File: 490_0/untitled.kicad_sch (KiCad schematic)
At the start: 31 parts, among them J2 PAD, J3 PAD, U16 SP3003-02XTG, U17 SP3003-02XTG, U4 USB2512B-I/M2, Y1 24M20P2/XT324-10/10

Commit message: Changed all the resistors to 0805 size
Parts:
- R11: footprint Resistor_THT:R_Axial_DIN0207_L6.3mm_D2.5mm_P10.16mm_Horizontal -> Resistor_SMD:R_0805_2012Metric; Digikey Link https://www.digikey.ca/en/products/detail/yageo/RC1206FR-07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 -> https://www.digikey.ca/en/products/detail/yageo/RC0805FR-13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; Manufacturer Part RC1206FR-0710KL -> RC0805FR-13330RL; Package 1206 -> 0805; Supplier P/N 311-10.0KFRCT-ND -> 13-RC0805FR-13330RLCT-ND; Unit (none) -> pcs
- R41: footprint Resistor_SMD:R_0603_1608Metric -> Resistor_SMD:R_0805_2012Metric; Digikey Link https://www.digikey.ca/en/products/detail/yageo/RC1206FR-07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 -> https://www.digikey.ca/en/products/detail/yageo/RC0805FR-07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; Manufacturer Part RC1206FR-071K5L -> RC0805FR-071K5L; Package 1206 -> 0805; Supplier P/N 311-1.50KFRCT-ND -> 311-1.50KCRCT-ND
- R42, R43, R46: footprint Resistor_THT:R_Axial_DIN0207_L6.3mm_D2.5mm_P10.16mm_Horizontal -> Resistor_SMD:R_0805_2012Metric; Digikey Link https://www.digikey.ca/en/products/detail/yageo/RC1206FR-07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 -> https://www.digikey.ca/en/products/detail/yageo/RC0805FR-07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; Manufacturer Part RC1206FR-0710KL -> RC0805FR-0710KL; Package 1206 -> 0805; Price 0.1 -> 0.14; Supplier P/N 311-10.0KFRCT-ND -> 311-10.0KCRCT-ND
- R45: footprint Resistor_SMD:R_0603_1608Metric -> Resistor_SMD:R_0805_2012Metric; Digikey Link https://www.digikey.ca/en/products/detail/yageo/RC1206FR-07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 -> https://www.digikey.ca/en/products/detail/yageo/RC0805FR-07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; Manufacturer Part RC1206FR-0710KL -> RC0805FR-0710KL; Package 1206 -> 0805; Price 0.1 -> 0.14; Supplier P/N 311-10.0KFRCT-ND -> 311-10.0KCRCT-ND
- R7: footprint Resistor_SMD:R_0603_1608Metric -> Resistor_SMD:R_0805_2012Metric; Digikey Link https://www.digikey.ca/en/products/detail/yageo/RC1206FR-07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 -> https://www.digikey.ca/en/products/detail/yageo/RC0805FR-07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; Manufacturer Part RC1206FR-0712KL -> RC0805FR-0712KL; Package 1206 -> 0805; Supplier P/N 311-12.0KFRCT-ND -> 311-12.0KCRCT-ND
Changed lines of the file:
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@@
 			)
 		)
-		(property "Footprint" "Resistor_SMD:R_0603_1608Metric"
+		(property "Footprint" "Resistor_SMD:R_0805_2012Metric"
 			(at 72.898 161.29 90)
 			(effects
@@
 			)
 		)
-		(property "Description" "RES 1.5K OHM 1% 1/4W 1206"
+		(property "Description" "RES 1.5K OHM 1% 1/8W 0805"
 			(at 71.12 161.29 0)
 			(effects
@@
 			)
 		)
-		(property "Digikey Link" "https://www.digikey.ca/en/products/detail/yageo/RC1206FR-071K5L/728441"
+		(property "Digikey Link" "https://www.digikey.ca/en/products/detail/yageo/RC0805FR-071K5L/727496"
 			(at 71.12 161.29 90)
 			(effects
@@
 			)
 		)
-		(property "Manufacturer Part" "RC1206FR-071K5L"
+		(property "Manufacturer Part" "RC0805FR-071K5L"
 			(at 71.12 161.29 90)
 			(effects
@@
 			)
 		)
-		(property "Supplier P/N" "311-1.50KFRCT-ND"
+		(property "Supplier P/N" "311-1.50KCRCT-ND"
 			(at 71.12 161.29 90)
 			(effects
@@
 			)
 		)
-		(property "Package" "1206"
+		(property "Package" "0805"
 			(at 71.12 161.29 90)
 			(effects
@@
 			)
 		)
-		(property "Footprint" "Resistor_THT:R_Axial_DIN0207_L6.3mm_D2.5mm_P10.16mm_Horizontal"
+		(property "Footprint" "Resistor_SMD:R_0805_2012Metric"
 			(at 88.138 173.101 0)
 			(effects
@@
 			)
 		)
-		(property "Description" "RES 10K OHM 1% 1/4W 1206"
+		(property "Description" "RES 10K OHM 1% 1/8W 0805"
 			(at 83.82 173.99 0)
 			(effects
@@
 			)
 		)
-		(property "Digikey Link" "https://www.digikey.ca/en/products/detail/yageo/RC1206FR-0710KL/728483"
+		(property "Digikey Link" "https://www.digikey.ca/en/products/detail/yageo/RC0805FR-0710KL/727535"
 			(at 83.82 173.99 0)
 			(effects
@@
 			)
 		)
-		(property "Manufacturer Part" "RC1206FR-0710KL"
+		(property "Manufacturer Part" "RC0805FR-0710KL"
 			(at 83.82 173.99 0)
 			(effects
@@
 			)
 		)
-		(property "Package" "1206"
+		(property "Package" "0805"
 			(at 83.82 173.99 0)
 			(effects
@@
 			)
 		)
-		(property "Price" "0.1"
+		(property "Price" "0.14"
 			(at 83.82 173.99 0)
 			(effects
@@
 			)
 		)
-		(property "Supplier P/N" "311-10.0KFRCT-ND"
+		(property "Supplier P/N" "311-10.0KCRCT-ND"
 			(at 83.82 173.99 0)
 			(effects
@@
 			)
 		)
-		(property "Footprint" "Resistor_THT:R_Axial_DIN0207_L6.3mm_D2.5mm_P10.16mm_Horizontal"
+		(property "Footprint" "Resistor_SMD:R_0805_2012Metric"
 			(at 44.958 160.401 0)
 			(effects
@@
 			)
 		)
-		(property "Description" "RES 10K OHM 1% 1/4W 1206"
+		(property "Description" "RES 10K OHM 1% 1/8W 0805"
 			(at 40.64 161.29 0)
 			(effects
@@
 			)
 		)
-		(property "Digikey Link" "https://www.digikey.ca/en/products/detail/yageo/RC1206FR-0710KL/728483"
+		(property "Digikey Link" "https://www.digikey.ca/en/products/detail/yageo/RC0805FR-0710KL/727535"
 			(at 40.64 161.29 0)
 			(effects
@@
 			)
 		)
-		(property "Manufacturer Part" "RC1206FR-0710KL"
+		(property "Manufacturer Part" "RC0805FR-0710KL"
 			(at 40.64 161.29 0)
 			(effects
@@
 			)
 		)
-		(property "Package" "1206"
+		(property "Package" "0805"
 			(at 40.64 161.29 0)
 			(effects
@@
 			)
 		)
-		(property "Price" "0.1"
+		(property "Price" "0.14"
 			(at 40.64 161.29 0)
 			(effects
@@
 			)
 		)
-		(property "Supplier P/N" "311-10.0KFRCT-ND"
+		(property "Supplier P/N" "311-10.0KCRCT-ND"
 			(at 40.64 161.29 0)
 			(effects
@@
 			)
 		)
-		(property "Footprint" "Resistor_SMD:R_0603_1608Metric"
+		(property "Footprint" "Resistor_SMD:R_0805_2012Metric"
 			(at 39.878 105.41 90)
 			(effects
@@
 			)
 		)
-		(property "Description" "RES 10K OHM 1% 1/4W 1206"
+		(property "Description" "RES 10K OHM 1% 1/8W 0805"
 			(at 38.1 105.41 0)
 			(effects
@@
 			)
 		)
-		(property "Digikey Link" "https://www.digikey.ca/en/products/detail/yageo/RC1206FR-0710KL/728483"
+		(property "Digikey Link" "https://www.digikey.ca/en/products/detail/yageo/RC0805FR-0710KL/727535"
 			(at 38.1 105.41 90)
 			(effects
@@
 			)
 		)
-		(property "Manufacturer Part" "RC1206FR-0710KL"
+		(property "Manufacturer Part" "RC0805FR-0710KL"
 			(at 38.1 105.41 90)
 			(effects
@@
 			)
 		)
-		(property "Supplier P/N" "311-10.0KFRCT-ND"
+		(property "Supplier P/N" "311-10.0KCRCT-ND"
 			(at 38.1 105.41 90)
 			(effects
@@
 			)
 		)
-		(property "Package" "1206"
+		(property "Package" "0805"
 			(at 38.1 105.41 90)
 			(effects
@@
 			)
 		)
-		(property "Price" "0.1"
+		(property "Price" "0.14"
 			(at 38.1 105.41 90)
 			(effects
@@
 			)
 		)
-		(property "Footprint" "Resistor_THT:R_Axial_DIN0207_L6.3mm_D2.5mm_P10.16mm_Horizontal"
+		(property "Footprint" "Resistor_SMD:R_0805_2012Metric"
 			(at 80.518 185.801 0)
 			(effects
@@
 			)
 		)
-		(property "Description" "RES 10K OHM 1% 1/4W 1206"
+		(property "Description" "RES 330 OHM 1% 1/8W 0805"
 			(at 76.2 186.69 0)
 			(effects
@@
 			)
 		)
-		(property "Digikey Link" "https://www.digikey.ca/en/products/detail/yageo/RC1206FR-0710KL/728483"
+		(property "Digikey Link" "https://www.digikey.ca/en/products/detail/yageo/RC0805FR-13330RL/14286486"
 			(at 76.2 186.69 0)
 			(effects
@@
 			)
 		)
-		(property "Manufacturer Part" "RC1206FR-0710KL"
+		(property "Manufacturer Part" "RC0805FR-13330RL"
 			(at 76.2 186.69 0)
 			(effects
@@
 			)
 		)
-		(property "Package" "1206"
+		(property "Package" "0805"
 			(at 76.2 186.69 0)
 			(effects
@@
 			)
 		)
-		(property "Supplier P/N" "311-10.0KFRCT-ND"
+		(property "Supplier P/N" "13-RC0805FR-13330RLCT-ND"
 			(at 76.2 186.69 0)
 			(effects
@@
 			)
 		)
-		(property "Unit" ""
+		(property "Unit" "pcs"
 			(at 76.2 186.69 0)
 			(effects
@@
 			)
 		)
-		(property "Footprint" "Resistor_THT:R_Axial_DIN0207_L6.3mm_D2.5mm_P10.16mm_Horizontal"
+		(property "Footprint" "Resistor_SMD:R_0805_2012Metric"
 			(at 60.198 160.401 0)
 			(effects
@@
 			)
 		)
-		(property "Description" "RES 10K OHM 1% 1/4W 1206"
+		(property "Description" "RES 10K OHM 1% 1/8W 0805"
 			(at 55.88 161.29 0)
 			(effects
@@
 			)
 		)
-		(property "Digikey Link" "https://www.digikey.ca/en/products/detail/yageo/RC1206FR-0710KL/728483"
+		(property "Digikey Link" "https://www.digikey.ca/en/products/detail/yageo/RC0805FR-0710KL/727535"
 			(at 55.88 161.29 0)
 			(effects
@@
 			)
 		)
-		(property "Manufacturer Part" "RC1206FR-0710KL"
+		(property "Manufacturer Part" "RC0805FR-0710KL"
 			(at 55.88 161.29 0)
 			(effects
@@
 			)
 		)
-		(property "Package" "1206"
+		(property "Package" "0805"
 			(at 55.88 161.29 0)
 			(effects
@@
 			)
 		)
-		(property "Price" "0.1"
+		(property "Price" "0.14"
 			(at 55.88 161.29 0)
 			(effects
@@
 			)
 		)
-		(property "Supplier P/N" "311-10.0KFRCT-ND"
+		(property "Supplier P/N" "311-10.0KCRCT-ND"
 			(at 55.88 161.29 0)
 			(effects
@@
 			)
 		)
-		(property "Footprint" "Resistor_SMD:R_0603_1608Metric"
+		(property "Footprint" "Resistor_SMD:R_0805_2012Metric"
 			(at 82.55 125.222 90)
 			(effects
@@
 			)
 		)
-		(property "Description" "RES 12K OHM 1% 1/4W 1206"
+		(property "Description" "RES 12K OHM 1% 1/8W 0805"
 			(at 82.55 127 0)
 			(effects
@@
 			)
 		)
-		(property "Digikey Link" "https://www.digikey.ca/en/products/detail/yageo/RC1206FR-0712KL/728516"
+		(property "Digikey Link" "https://www.digikey.ca/en/products/detail/yageo/RC0805FR-0712KL/727568"
 			(at 82.55 127 90)
 			(effects
@@
 			)
 		)
-		(property "Manufacturer Part" "RC1206FR-0712KL"
+		(property "Manufacturer Part" "RC0805FR-0712KL"
 			(at 82.55 127 90)
 			(effects
@@
 			)
 		)
-		(property "Supplier P/N" "311-12.0KFRCT-ND"
+		(property "Supplier P/N" "311-12.0KCRCT-ND"
 			(at 82.55 127 90)
 			(effects
@@
 			)
 		)
-		(property "Package" "1206"
+		(property "Package" "0805"
 			(at 82.55 127 90)
 			(effects

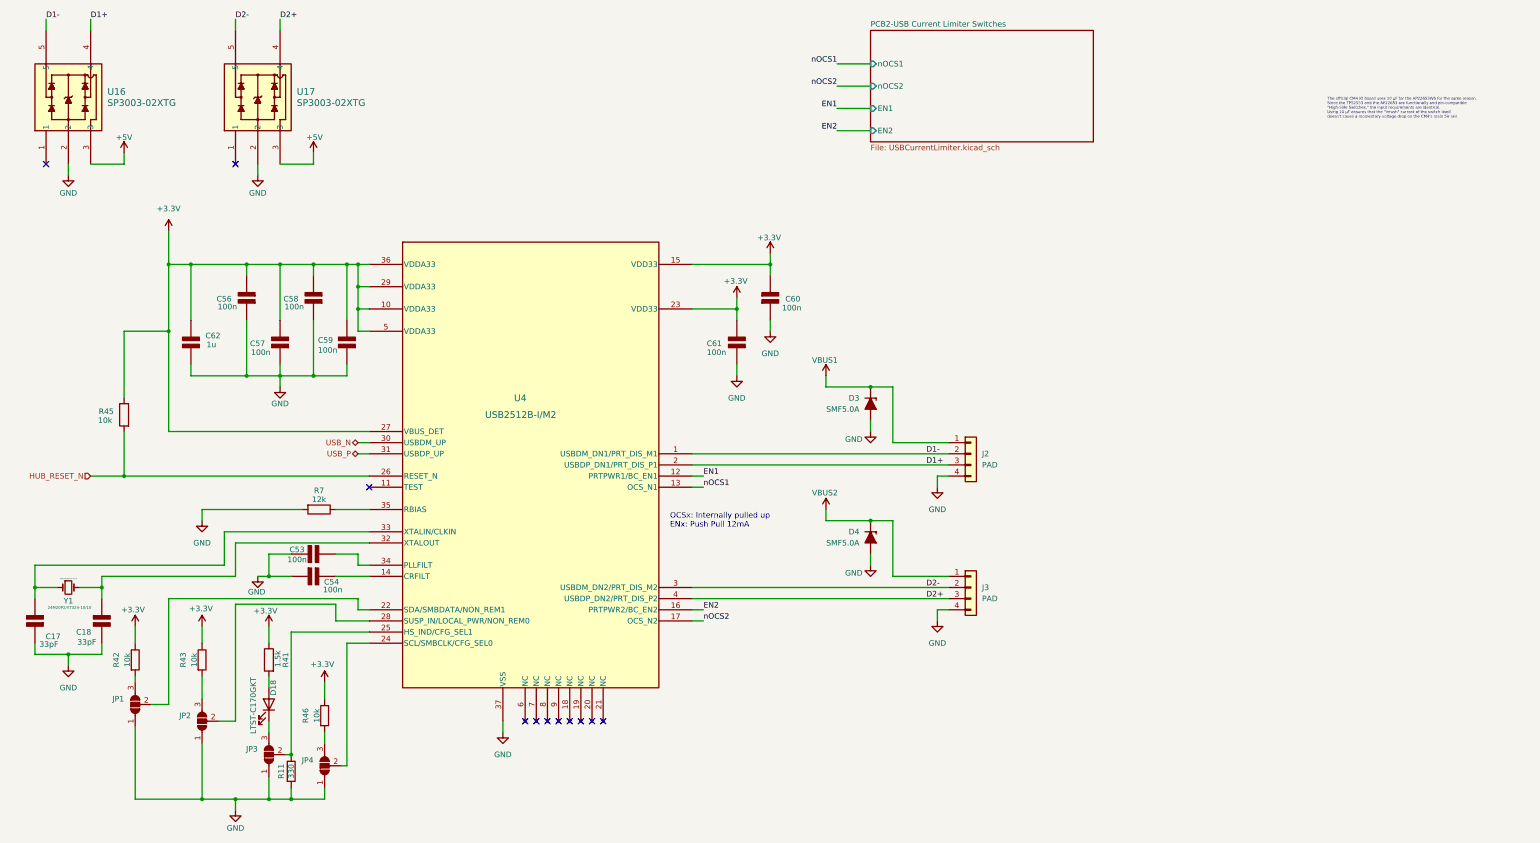
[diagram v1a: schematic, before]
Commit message: changed power and ground symbols for glasses
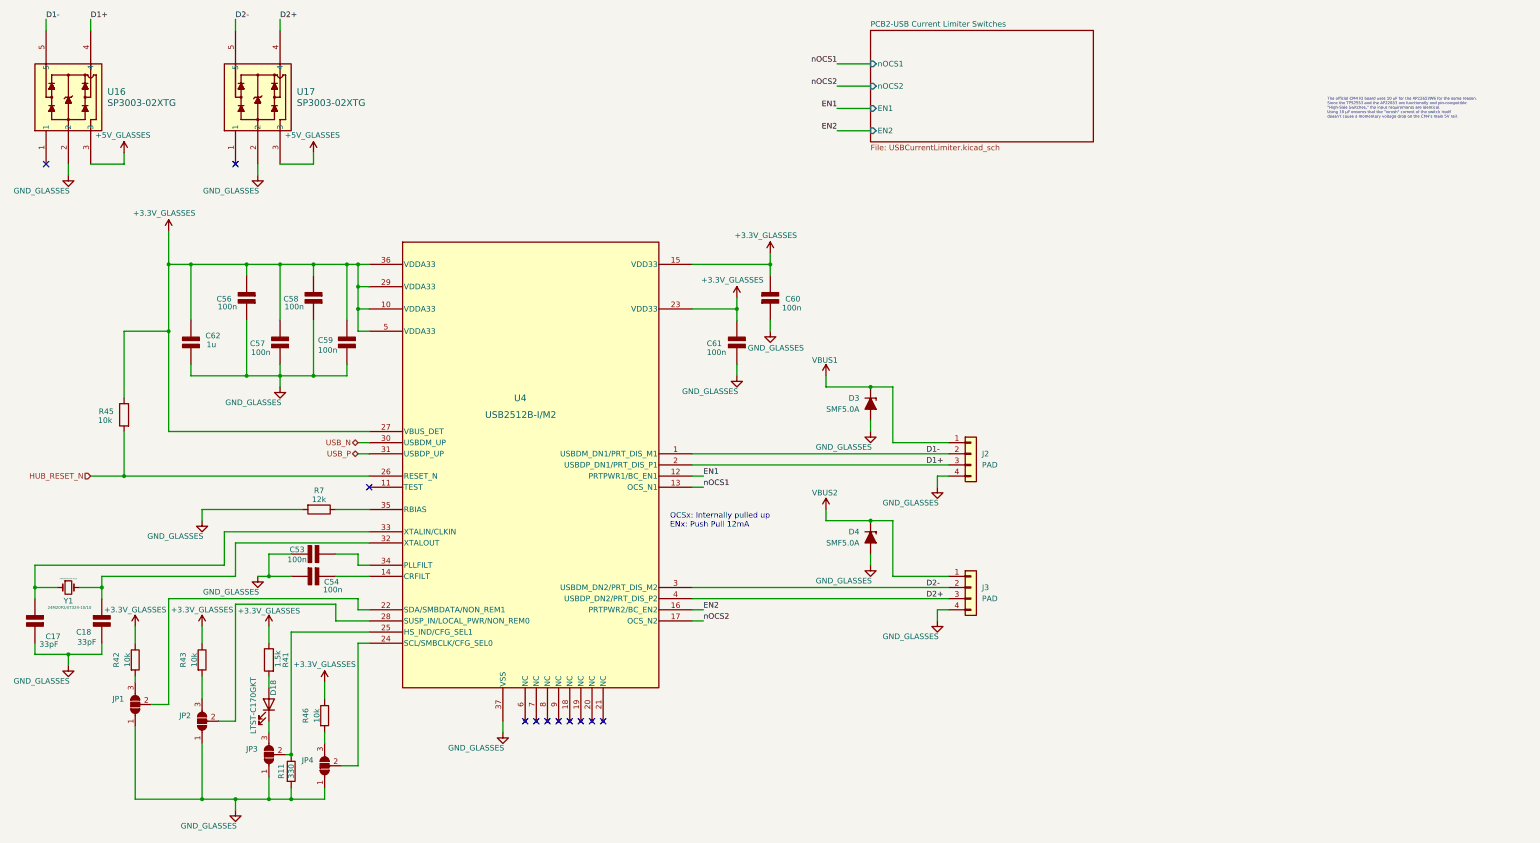
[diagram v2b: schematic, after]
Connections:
- net +3.3V renamed +3.3V_GLASSES
- net +5V renamed +5V_GLASSES
- net GND renamed GND_GLASSES

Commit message: Generated BOM
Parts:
- J2, J3, JP1, JP2, JP3, JP4: now in the parts list
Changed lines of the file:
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@@
 		(unit 1)
 		(exclude_from_sim no)
-		(in_bom no)
+		(in_bom yes)
 		(on_board yes)
 		(dnp no)
@@
 		(unit 1)
 		(exclude_from_sim no)
-		(in_bom no)
+		(in_bom yes)
 		(on_board yes)
 		(dnp no)
@@
 		(unit 1)
 		(exclude_from_sim no)
-		(in_bom no)
+		(in_bom yes)
 		(on_board yes)
 		(dnp no)
@@
 		(unit 1)
 		(exclude_from_sim no)
-		(in_bom no)
+		(in_bom yes)
 		(on_board yes)
 		(dnp no)
@@
 		(unit 1)
 		(exclude_from_sim no)
-		(in_bom no)
+		(in_bom yes)
 		(on_board yes)
 		(dnp no)
@@
 		(unit 1)
 		(exclude_from_sim no)
-		(in_bom no)
+		(in_bom yes)
 		(on_board yes)
 		(dnp no)

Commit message: Added side B for SW1
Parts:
- C17, C18, C53, C54, C56, C57, C58, C59, C60, C61, C62: symbol PCM_Elektuur:C -> capstone_parts:C
- D18: symbol Device:LED -> capstone_parts:LED
- D3, D4: symbol PCM_Diode_TVS_AKL:SMF5.0A -> capstone_parts:SMF5.0A
- J2, J3: symbol PCM_SparkFun-Connector:Conn_01x04_P2.54mm -> capstone_parts:Conn_01x04_P2.54mm
- JP1, JP2, JP3, JP4: symbol Jumper:SolderJumper_3_Open -> capstone_parts:SolderJumper_3_Open
- R11, R42, R43, R46: symbol PCM_SL_Resistors:Resistor -> capstone_parts:Resistor
- R41, R45, R7: symbol Device:R -> capstone_parts:R
- Y1: symbol PCM_SparkFun-Clock:Crystal -> capstone_parts:Crystal
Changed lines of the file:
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@@
 	)
 	(symbol
-		(lib_id "Jumper:SolderJumper_3_Open")
+		(lib_id "capstone_parts:SolderJumper_3_Open")
 		(at 40.64 171.45 90)
 		(unit 1)
@@
 	)
 	(symbol
-		(lib_id "PCM_Elektuur:C")
+		(lib_id "capstone_parts:C")
 		(at 177.8 88.9 180)
 		(unit 1)
@@
 	)
 	(symbol
-		(lib_id "PCM_Elektuur:C")
+		(lib_id "capstone_parts:C")
 		(at 88.9 88.9 180)
 		(unit 1)
@@
 	)
 	(symbol
-		(lib_id "PCM_Elektuur:C")
+		(lib_id "capstone_parts:C")
 		(at 53.34 88.9 180)
 		(unit 1)
@@
 	)
 	(symbol
-		(lib_id "Jumper:SolderJumper_3_Open")
+		(lib_id "capstone_parts:SolderJumper_3_Open")
 		(at 55.88 175.26 90)
 		(unit 1)
@@
 	)
 	(symbol
-		(lib_id "PCM_SparkFun-Connector:Conn_01x04_P2.54mm")
+		(lib_id "capstone_parts:Conn_01x04_P2.54mm")
 		(at 231.14 144.78 0)
 		(unit 1)
@@
 	)
 	(symbol
-		(lib_id "Jumper:SolderJumper_3_Open")
+		(lib_id "capstone_parts:SolderJumper_3_Open")
 		(at 83.82 185.42 90)
 		(unit 1)
@@
 	)
 	(symbol
-		(lib_id "PCM_Elektuur:C")
+		(lib_id "capstone_parts:C")
 		(at 81.28 142.24 90)
 		(mirror x)
@@
 	)
 	(symbol
-		(lib_id "PCM_Elektuur:C")
+		(lib_id "capstone_parts:C")
 		(at 66.04 78.74 180)
 		(unit 1)
@@
 	)
 	(symbol
-		(lib_id "Device:R")
+		(lib_id "capstone_parts:R")
 		(at 71.12 161.29 0)
 		(mirror y)
@@
 	)
 	(symbol
-		(lib_id "PCM_SL_Resistors:Resistor")
+		(lib_id "capstone_parts:Resistor")
 		(at 83.82 173.99 90)
 		(unit 1)
@@
 	)
 	(symbol
-		(lib_id "PCM_Diode_TVS_AKL:SMF5.0A")
+		(lib_id "capstone_parts:SMF5.0A")
 		(at 208.28 133.35 270)
 		(mirror x)
@@
 	)
 	(symbol
-		(lib_id "PCM_Elektuur:C")
+		(lib_id "capstone_parts:C")
 		(at 81.28 137.16 90)
 		(mirror x)
@@
 	)
 	(symbol
-		(lib_id "Device:LED")
+		(lib_id "capstone_parts:LED")
 		(at 71.12 171.45 270)
 		(mirror x)
@@
 	)
 	(symbol
-		(lib_id "PCM_SparkFun-Connector:Conn_01x04_P2.54mm")
+		(lib_id "capstone_parts:Conn_01x04_P2.54mm")
 		(at 231.14 114.3 0)
 		(unit 1)
@@
 	)
 	(symbol
-		(lib_id "PCM_SparkFun-Clock:Crystal")
+		(lib_id "capstone_parts:Crystal")
 		(at 25.4 144.78 0)
 		(mirror x)
@@
 	)
 	(symbol
-		(lib_id "PCM_SL_Resistors:Resistor")
+		(lib_id "capstone_parts:Resistor")
 		(at 40.64 161.29 90)
 		(unit 1)
@@
 	)
 	(symbol
-		(lib_id "Device:R")
+		(lib_id "capstone_parts:R")
 		(at 38.1 105.41 0)
 		(mirror y)
@@
 	)
 	(symbol
-		(lib_id "PCM_Diode_TVS_AKL:SMF5.0A")
+		(lib_id "capstone_parts:SMF5.0A")
 		(at 208.28 102.87 270)
 		(mirror x)
@@
 	)
 	(symbol
-		(lib_id "PCM_Elektuur:C")
+		(lib_id "capstone_parts:C")
 		(at 73.66 88.9 180)
 		(unit 1)
@@
 	)
 	(symbol
-		(lib_id "PCM_SL_Resistors:Resistor")
+		(lib_id "capstone_parts:Resistor")
 		(at 76.2 186.69 90)
 		(unit 1)
@@
 	)
 	(symbol
-		(lib_id "Jumper:SolderJumper_3_Open")
+		(lib_id "capstone_parts:SolderJumper_3_Open")
 		(at 71.12 182.88 90)
 		(unit 1)
@@
 	)
 	(symbol
-		(lib_id "PCM_Elektuur:C")
+		(lib_id "capstone_parts:C")
 		(at 185.42 78.74 0)
 		(mirror x)
@@
 	)
 	(symbol
-		(lib_id "PCM_Elektuur:C")
+		(lib_id "capstone_parts:C")
 		(at 33.02 152.4 0)
 		(unit 1)
@@
 	)
 	(symbol
-		(lib_id "PCM_SL_Resistors:Resistor")
+		(lib_id "capstone_parts:Resistor")
 		(at 55.88 161.29 90)
 		(unit 1)
@@
 	)
 	(symbol
-		(lib_id "PCM_Elektuur:C")
+		(lib_id "capstone_parts:C")
 		(at 81.28 78.74 180)
 		(unit 1)
@@
 	)
 	(symbol
-		(lib_id "Device:R")
+		(lib_id "capstone_parts:R")
 		(at 82.55 127 270)
 		(unit 1)
@@
 	)
 	(symbol
-		(lib_id "PCM_Elektuur:C")
+		(lib_id "capstone_parts:C")
 		(at 17.78 152.4 0)
 		(mirror y)

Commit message: Rerouted + external coponents update
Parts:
- added C31: 100n, Capacitor_SMD:C_0603_1608Metric, symbol capstone_parts:C
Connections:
- net GND_GLASSES: now also C31.1 (+)
- net HUB_RESET_N: no longer names the net of R45.2, U4.26 (RESET_N)
- net HUB_RESET_N: now also C31.2 (-)
